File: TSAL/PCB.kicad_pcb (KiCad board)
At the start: 4 copper layers, 29.2 x 51.1 mm, 35 parts, among them J1 Conn_01x15, J2 USB_C_Receptacle_USB2.0, J3 Conn_01x15, J4 TC2030, J5 Conn_01x04, SW1 SW_Push, SW2 SW_Push, U1 SN65HVD230, U2 AMS1117-3.3, U3 STM32F103C8T6, Y1 8MHz

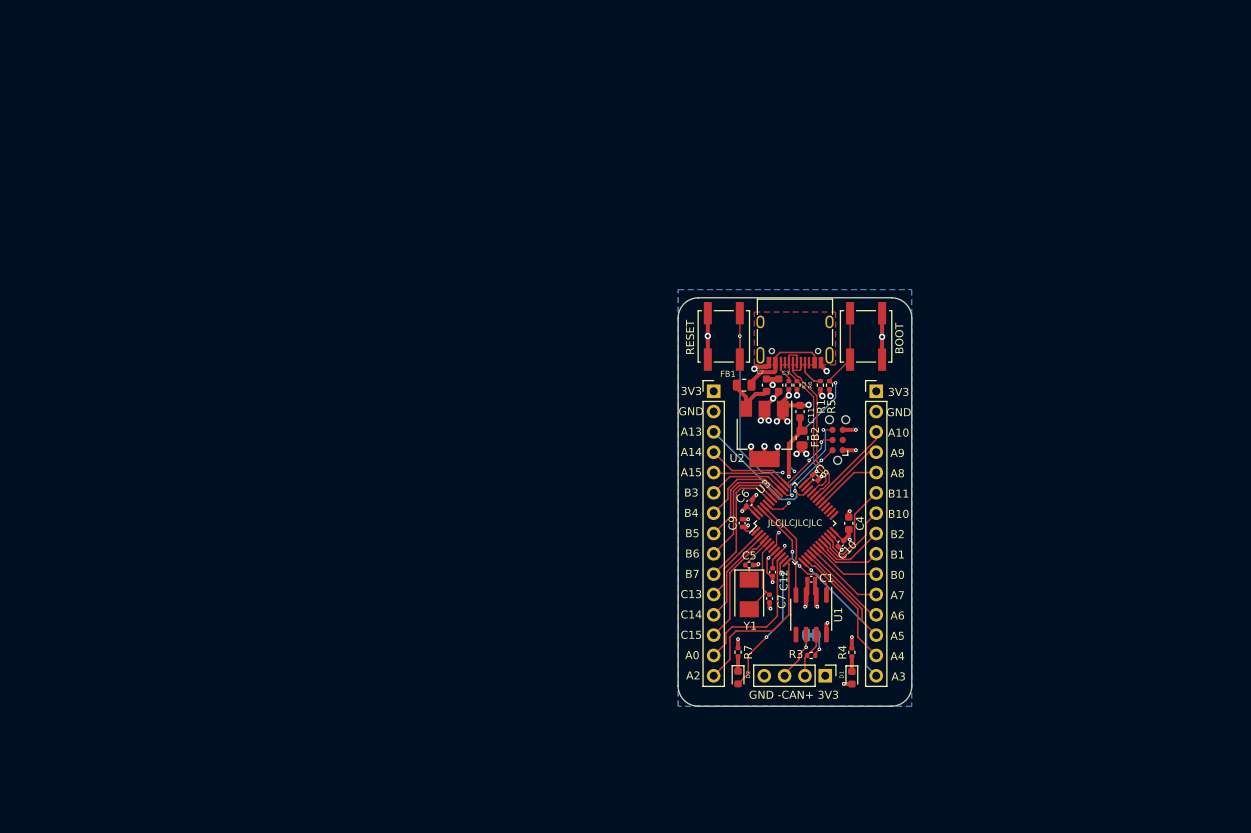
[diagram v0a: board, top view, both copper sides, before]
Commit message: Changed opto-isolator
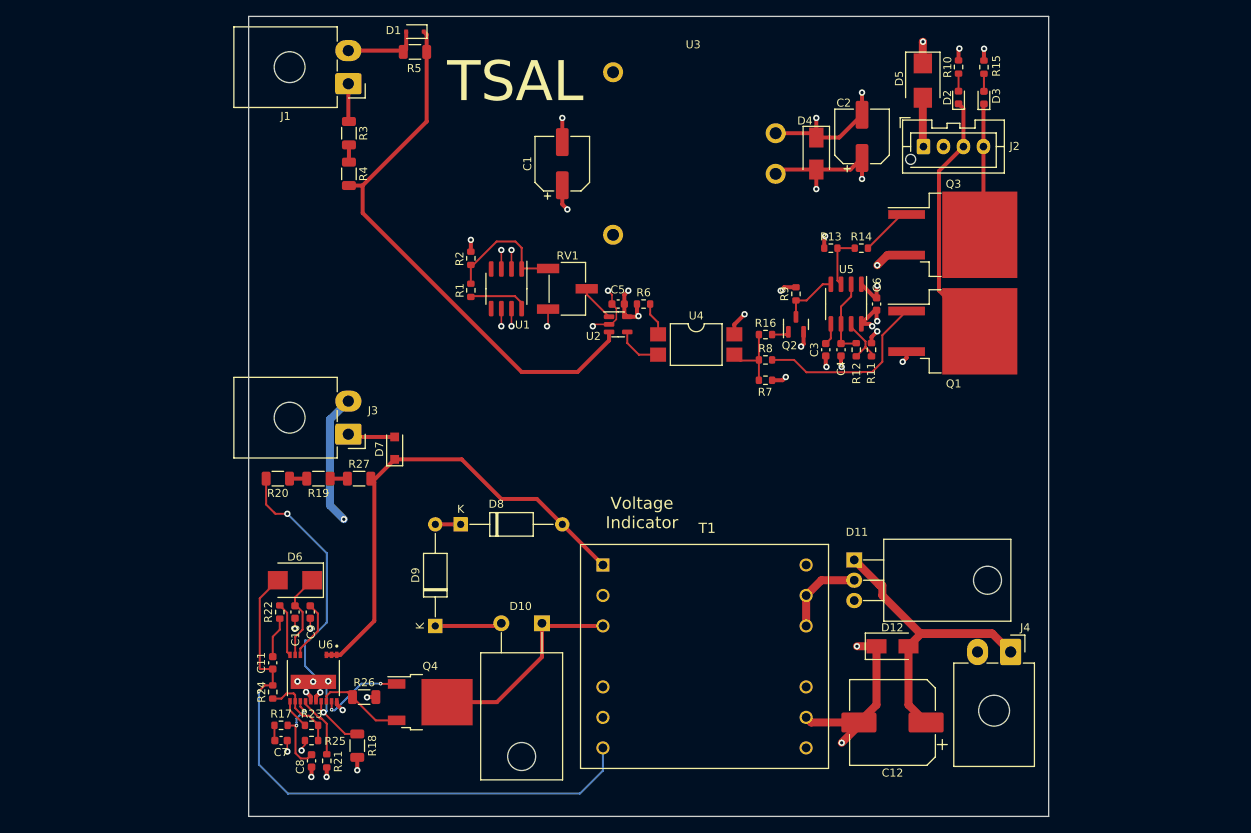
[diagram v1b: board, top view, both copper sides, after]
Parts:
- removed FB1, FB2: 100R@100MHz, Resistor_SMD:R_0805_2012Metric
- removed J5: Conn_01x04, Connector_PinHeader_2.54mm:PinHeader_1x04_P2.54mm_Vertical
- removed JP1: SolderJumper_Bridged, Jumper:SolderJumper-2_P1.3mm_Bridged_RoundedPad1.0x1.5mm
- removed SW1, SW2: SW_Push, Button_Switch_SMD:SW_Push_1P1T_NO_CK_KSC7xxJ
- removed Y1: 8MHz, Crystal:Crystal_SMD_5032-2Pin_5.0x3.2mm
- added D10: RFN5TF8S, Package_TO_SOT_THT:TO-220-2_Horizontal_TabDown, F.Cu at (115.7, 117.9)
- added D11: RB238T150, Package_TO_SOT_THT:TO-220-3_Horizontal_TabDown, F.Cu at (154.7, 110.0)
- added D12: SMAJ15CA, Diode_SMD:D_SMA, F.Cu at (159.5, 120.8)
- added D3: LED-Red, LED_SMD:LED_0603_1608Metric, F.Cu at (170.9, 52.2)
- added D4: SMAJ15CA, Diode_SMD:D_SMA, F.Cu at (150.0, 59.2)
- added D5: SSB43L, Diode_SMD:D_SMB, F.Cu at (163.3, 50.1)
- added D6: SK520B, Diode_SMD:D_SMB, F.Cu at (84.8, 112.5)
- added D7: 1N4007FL, Diode_SMD:D_SOD-123F, F.Cu at (97.3, 96.0)
- added D8: 1N5375B, Diode_THT:D_A-405_P12.70mm_Horizontal, F.Cu at (105.5, 105.5)
- added D9: 1N5375B, Diode_THT:D_A-405_P12.70mm_Horizontal, F.Cu at (102.4, 118.2)
- added Q1: IRLZ44N, Package_TO_SOT_SMD:TO-263-2, F.Cu at (167.0, 81.4)
- added Q2: MMBT3904, Package_TO_SOT_SMD:SOT-23, F.Cu at (147.4, 80.5)
- added Q3: IRLZ44N, Package_TO_SOT_SMD:TO-263-2, F.Cu at (167.0, 69.3)
- added Q4: STD7NK40Z, Package_TO_SOT_SMD:TO-252-2, F.Cu at (101.7, 127.8)
- added R10: 2.2k, Resistor_SMD:R_0603_1608Metric, F.Cu at (167.8, 48.4)
- added R11: 22k, Resistor_SMD:R_0603_1608Metric, F.Cu at (156.9, 83.7)
- added R12: 220k, Resistor_SMD:R_0603_1608Metric, F.Cu at (155.0, 83.7)
- added R13: 100k, Resistor_SMD:R_0603_1608Metric, F.Cu at (151.8, 71.0)
- added R14: 1k, Resistor_SMD:R_0603_1608Metric, F.Cu at (155.6, 71.0)
- added R15: 2.2k, Resistor_SMD:R_0603_1608Metric, F.Cu at (170.9, 48.4)
- added R16: 22k, Resistor_SMD:R_0603_1608Metric, F.Cu at (143.6, 81.8)
- added R17: 10k, Resistor_SMD:R_0603_1608Metric, F.Cu at (83.1, 130.7)
- added R18: 40k, Resistor_SMD:R_1206_3216Metric, F.Cu at (92.6, 133.2)
- added R19: 500k, Resistor_SMD:R_1206_3216Metric, F.Cu at (87.8, 99.8)
- added R20: 500k, Resistor_SMD:R_1206_3216Metric, F.Cu at (82.7, 99.8)
- added R21: 56.2k, Resistor_SMD:R_0603_1608Metric, F.Cu at (88.8, 135.1)
- added R22: 10k, Resistor_SMD:R_0603_1608Metric, F.Cu at (82.9, 116.5)
- added R23: 121k, Resistor_SMD:R_0603_1608Metric, F.Cu at (86.9, 130.7)
- added R24: 44.2k, Resistor_SMD:R_0603_1608Metric, F.Cu at (82.0, 126.5)
- added R25: 4.99k, Resistor_SMD:R_0603_1608Metric, F.Cu at (86.9, 132.6)
- added R26: 0.05, Resistor_SMD:R_1206_3216Metric, F.Cu at (93.5, 127.1)
- added R27: 500k, Resistor_SMD:R_1206_3216Metric, F.Cu at (92.8, 99.8)
- added R8: 1k, Resistor_SMD:R_0603_1608Metric, F.Cu at (143.6, 85.0)
- added R9: 22k, Resistor_SMD:R_0603_1608Metric, F.Cu at (147.4, 76.7)
- added RV1: 10k, Potentiometer_SMD:Potentiometer_Bourns_3269W_Vertical, F.Cu at (118.9, 76.1)
- added T1: 11328-T078, 11328-T078:11328T078, F.Cu at (123.3, 110.6)
- added U4: LTV-817S, Package_DIP:SMDIP-4_W9.53mm, F.Cu at (135.0, 83.1)
- added U5: LM555xN, Package_SO:SOIC-8_3.9x4.9mm_P1.27mm, F.Cu at (153.7, 78.0)
- added U6: LT8316IFE#PBF, kicad-libraries:IC_LT8316IFE#PBF, F.Cu at (87.1, 124.8)
- C1: value 100n -> 100u; footprint Capacitor_SMD:C_0402_1005Metric -> Capacitor_SMD:CP_Elec_6.3x7.7
- C10, C9: value 100n -> 4.7u; footprint Capacitor_SMD:C_0402_1005Metric -> Capacitor_SMD:C_0603_1608Metric
- C11: value 1u -> 47p
- C12: value 100n -> 470uF; footprint Capacitor_SMD:C_0402_1005Metric -> Capacitor_SMD:CP_Elec_10x10.5
- C2: value 1u -> 100u; footprint Capacitor_SMD:C_0603_1608Metric -> Capacitor_SMD:CP_Elec_6.3x7.7
- C3: value 1u -> 100nF
- C4: value 4u7 -> 1microF
- C5: value 30p -> 100nF; footprint Capacitor_SMD:C_0402_1005Metric -> Capacitor_SMD:C_0603_1608Metric
- C6: value 100n -> 100nF; footprint Capacitor_SMD:C_0402_1005Metric -> Capacitor_SMD:C_0603_1608Metric
- C7: value 30p -> 0.1u; footprint Capacitor_SMD:C_0402_1005Metric -> Capacitor_SMD:C_0603_1608Metric
- C8: value 100n -> 47p; footprint Capacitor_SMD:C_0402_1005Metric -> Capacitor_SMD:C_0603_1608Metric
- D1: value YELLOW -> BZT52C5V1SQ-7-F; footprint LED_SMD:LED_0603_1608Metric -> Diode_SMD:D_SOD-323F
- D2: value BLUE -> LED-Green
- J1, J3: value Conn_01x15 -> TE 770966-2; footprint Connector_PinHeader_2.54mm:PinHeader_1x15_P2.54mm_Vertical -> Connector_TE-Connectivity:TE_MATE-N-LOK_1-770966-x_1x02_P4.14mm_Horizontal
- J2: value USB_C_Receptacle_USB2.0 -> JST B04B-XASK; footprint Connector_USB:USB_C_Receptacle_HRO_TYPE-C-31-M-12 -> Connector_JST:JST_XA_B04B-XASK-1-A_1x04_P2.50mm_Vertical
- J4: value TC2030 -> TE 770966-2; footprint Connector:Tag-Connect_TC2030-IDC-NL_2x03_P1.27mm_Vertical -> Connector_TE-Connectivity:TE_MATE-N-LOK_1-770966-x_1x02_P4.14mm_Horizontal
- R1, R2: value 5k1 -> 2.2k; footprint Resistor_SMD:R_0402_1005Metric -> Resistor_SMD:R_0603_1608Metric
- R3: value 120R -> 1M; footprint Resistor_SMD:R_0402_1005Metric -> Resistor_SMD:R_1206_3216Metric
- R4: value 1k5 -> 1M; footprint Resistor_SMD:R_0402_1005Metric -> Resistor_SMD:R_1206_3216Metric
- R5: value 5k1 -> 20K; footprint Resistor_SMD:R_0402_1005Metric -> Resistor_SMD:R_1206_3216Metric
- R6: value 1k5 -> 2.2k; footprint Resistor_SMD:R_0402_1005Metric -> Resistor_SMD:R_0603_1608Metric
- R7: value 1k5 -> 100k; footprint Resistor_SMD:R_0402_1005Metric -> Resistor_SMD:R_0603_1608Metric
- U1: value SN65HVD230 -> TL431D
- U2: value AMS1117-3.3 -> LMV331; footprint Package_TO_SOT_SMD:SOT-223-3_TabPin2 -> Package_TO_SOT_SMD:SOT-23-5
- U3: value STM32F103C8T6 -> VRB1205YMD-6WR3; footprint Package_QFP:LQFP-48_7x7mm_P0.5mm -> VRB1205YMD-6WR3:VRB1205YMD-6WR3
- moved D1 97.5 mm to (99.8, 43.9), turned to 180 degrees
- moved R3 87.2 mm to (91.6, 56.6), turned to -90 degrees
- moved R4 86.8 mm to (91.6, 61.7), turned to -90 degrees
- moved D2 77.6 mm to (167.8, 52.2), turned to 90 degrees
- moved C11 73.0 mm to (82.0, 122.8)
- moved C8 72.2 mm to (86.9, 135.1), turned to -90 degrees
- moved C10 68.7 mm to (84.8, 116.5), turned to 90 degrees
- moved R5 66.5 mm to (99.8, 46.5), turned to 180 degrees
- moved J3 66.2 mm to (91.5, 94.3), turned to 180 degrees
- moved C7 63.6 mm to (83.1, 132.6), turned to 0 degrees
- moved C1 60.5 mm to (118.2, 60.5), turned to 90 degrees
- moved J1 59.7 mm to (91.5, 50.5), turned to 180 degrees
- moved U1 55.8 mm to (111.3, 76.1)
- moved C9 55.1 mm to (86.7, 116.5)
- moved U3 47.9 mm to (134.7, 59.2), turned to 180 degrees
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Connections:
- C1 pad 1: +3V3 -> +5V
- C1 pad 2: GND -> TS-
- C10 pad 1: +3V3 -> VI-
- C10 pad 2: GND -> Net-(C10-Pad2)
- C11 pad 1: +3.3VA -> Net-(C11-Pad1)
- C11 pad 2: GND -> Net-(C11-Pad2)
- C12 pad 1: +3.3VA -> Net-(C12-Pad1)
- C2 pad 1: VCC -> +12V
- C3 pad 1: +3V3 -> GND
- C3 pad 2: GND -> Net-(C3-Pad2)
- C4 pad 1: +3V3 -> Net-(C4-Pad1)
- C5 pad 1: /HSE_OUT -> +5V
- C5 pad 2: GND -> TS-
- C6 pad 1: +3V3 -> +12V
- C7 pad 1: /HSE_IN -> Net-(C7-Pad1)
- C7 pad 2: GND -> VI-
- C8 pad 1: +3V3 -> Net-(C8-Pad1)
- C8 pad 2: GND -> VI-
- C9 pad 1: +3V3 -> VI-
- C9 pad 2: GND -> Net-(C9-Pad2)
- D1 pad 2: +3V3 -> TS-
- D2 pad 1: Net-(D2-Pad1) -> /Ext-LED-Green
- D2 pad 2: /LED_STAT -> Net-(D2-Pad2)
- J1 pad 1: +3V3 -> TS+
- J1 pad 2: GND -> TS-
- J3 pad 1: +3V3 -> Net-(D7-Pad2)
- J3 pad 2: GND -> VI-
- J4 pad 1: +3V3 -> Net-(C12-Pad1)
- J4 pad 2: SWDIO -> GND
- R1 pad 1: Net-(J2-PadA5) -> Net-(R1-Pad1)
- R1 pad 2: GND -> Net-(R1-Pad2)
- R2 pad 1: GND -> +5V
- R2 pad 2: Net-(J2-PadB5) -> Net-(R1-Pad1)
- R3 pad 1: /CAN+ -> TS+
- R3 pad 2: Net-(JP1-Pad2) -> Net-(R3-Pad2)
- R4 pad 1: Net-(D1-Pad1) -> Net-(R3-Pad2)
- R4 pad 2: GND -> Net-(D1-Pad1)
- R5 pad 1: /BOOT0 -> Net-(D1-Pad1)
- R5 pad 2: GND -> TS-
- R6 pad 1: +3V3 -> +5V
- R6 pad 2: USB_D+ -> Net-(R6-Pad2)
- R7 pad 1: Net-(D2-Pad1) -> Net-(R16-Pad1)
- U1 pad 1: CANTX -> Net-(R1-Pad1)
- U1 pad 2: GND -> TS-
- U1 pad 3: +3V3 -> TS-
- U1 pad 4: CANRX -> (no net)
- U1 pad 5: unconnected-(U1-Pad5) -> (no net)
- U1 pad 6: /CAN- -> TS-
- U1 pad 7: /CAN+ -> TS-
- U1 pad 8: GND -> Net-(R1-Pad2)
- U2 pad 1: GND -> Net-(RV1-Pad2)
- U2 pad 2: +3V3 -> TS-
- U2 pad 3: VCC -> Net-(D1-Pad1)
- U3 pad 1: +3V3 -> GND
- U3 pad 2: PC13 -> +12V
- U3 pad 3: PC14 -> +5V
- U3 pad 5: /HSE_OUT -> TS-
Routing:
- net Net-(C11-Pad1): track 0.00 -> 75.4 mm, vias 0 -> 1
- net Net-(D1-Pad1): track 1.88 -> 69.6 mm
- net VI+: track 0.00 -> 61.2 mm
- net Net-(C12-Pad1): track 0.00 -> 46.6 mm
- net +3V3: track 44.0 -> 0.00 mm, vias 18 -> 0
- net Net-(R18-Pad2): track 0.00 -> 42.9 mm, vias 0 -> 2
- net /NRST: track 35.9 -> 0.00 mm, vias 3 -> 0
- net +12V: track 0.00 -> 34.8 mm, vias 0 -> 10
- net /Ext-LED-Green: track 0.00 -> 32.1 mm
- net /BOOT0: track 31.5 -> 0.00 mm, vias 3 -> 0
- net TS-: track 0.00 -> 31.3 mm, vias 0 -> 8
- net VI-: track 0.00 -> 31.2 mm, vias 0 -> 15
- net Net-(D10-Pad1): track 0.00 -> 26.2 mm
- net SWDIO: track 24.1 -> 0.00 mm, vias 2 -> 0
- net SWO: track 22.9 -> 0.00 mm, vias 2 -> 0
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- added copper zone on In2.Cu, net +12V
- added copper zone on In2.Cu, net +5V
- added copper zone on In1.Cu, net TS-
- added copper zone on In1.Cu, net VI-
- removed copper zone on In2.Cu, net +3V3
- removed copper zone on B.Cu, net GND
- removed copper zone on F.Cu, net unconnected-(J2-PadS1)
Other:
- board size 29.2 x 51.1 mm -> 100 x 100 mm
- board text added: "TSAL"
- board text added: "Voltage Indicator"
- board text removed: "3V3"
- board text removed: "3V3 +CAN- GND"
- board text removed: "A0"
- board text removed: "A10"
- board text removed: "A13"
- board text removed: "A14"
- board text removed: "A15"
- board text removed: "A2"
- board text removed: "A3"
- board text removed: "A4"
- board text removed: "A5"
- board text removed: "A6"
- board text removed: "A7"
- board text removed: "A8"
- board text removed: "A9"
- board text removed: "B0"
- board text removed: "B1"
- board text removed: "B10"
- board text removed: "B11"
- board text removed: "B2"
- board text removed: "B3"
- board text removed: "B4"
- board text removed: "B5"
- board text removed: "B6"
- board text removed: "B7"
- board text removed: "BOOT"
- board text removed: "C13"
- board text removed: "C14"
- board text removed: "C15"
- board text removed: "CAN TERM"
- board text removed: "GND"
- board text removed: "GND -CAN+ 3V3"
- board text removed: "JLCJLCJLCJLC"
- board text removed: "RESET"
- board text removed: "Rev 1"
- board text removed: "STM32F103 CAN/USB-C Jack LeFevre July 2022"
- board text removed: "SWCLK"
- board text removed: "SWDIO"
- board text removed: "SWO"

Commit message: TSAL - meme
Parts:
- added REF**: MountingHole_3.2mm_M3_ISO14580, MountingHole:MountingHole_3.2mm_M3_ISO14580, F.Cu at (156.0, 139.0)
- added REF**: MountingHole_3.2mm_M3_ISO14580, MountingHole:MountingHole_3.2mm_M3_ISO14580, F.Cu at (170.0, 98.0)
- added REF**: MountingHole_3.2mm_M3_ISO14580, MountingHole:MountingHole_3.2mm_M3_ISO14580, F.Cu at (86.0, 75.0)
- added REF**: MountingHole_3.2mm_M3_ISO14580, MountingHole:MountingHole_3.2mm_M3_ISO14580, F.Cu at (154.0, 47.0)
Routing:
- net Net-(R18-Pad2): track 42.9 -> 40.9 mm
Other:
- board text added: "12V GND GRN RED"
- board text added: "Bronco Racing TSAL + Voltage Indicator Rev 1"
- board text added: "GND"
- board text added: "Grounded Low Voltage"
- board text added: "High Voltage"
- board text added: "Josh Iwick Feb 2023"
- board text added: "TS+"
- board text added: "TS-"
- board text added: "TSAL HV In"
- board text added: "VI 12V"
- board text added: "Voltage Indicator In"

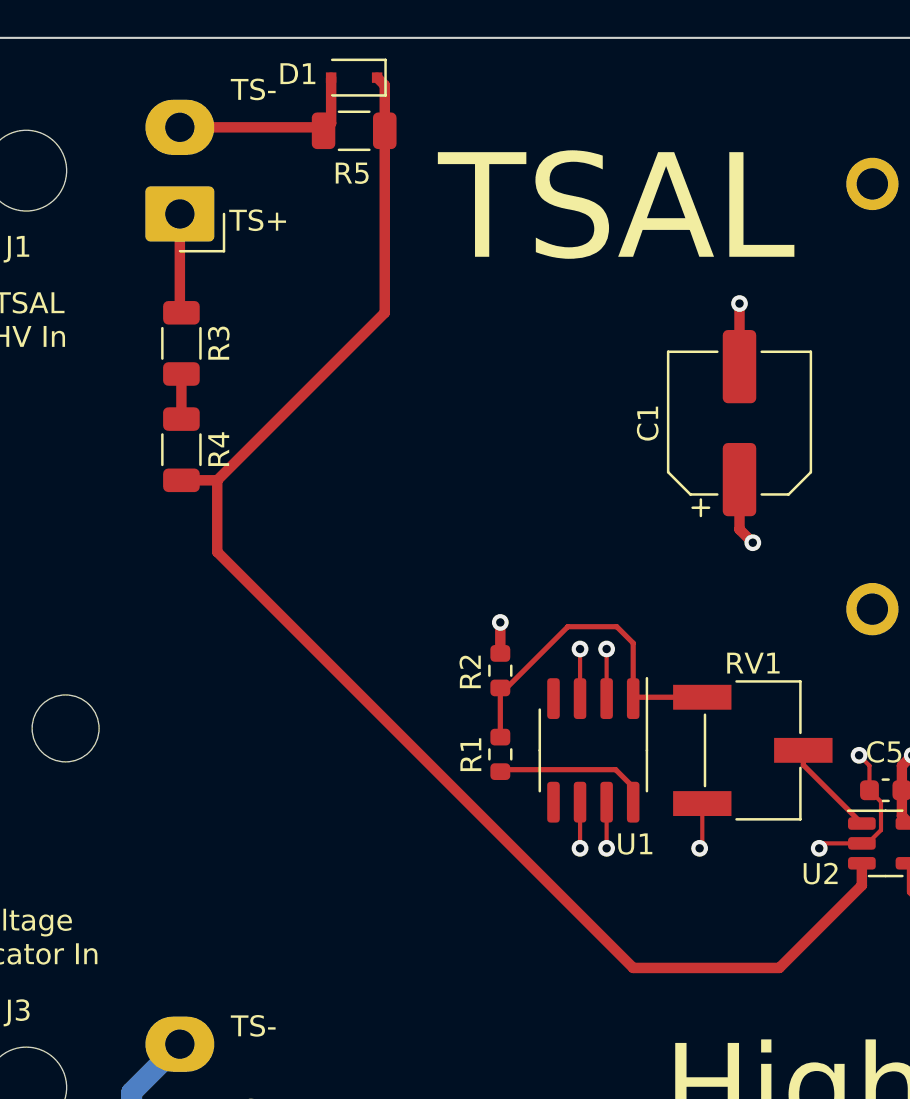
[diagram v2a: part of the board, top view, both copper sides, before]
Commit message: resisitor change
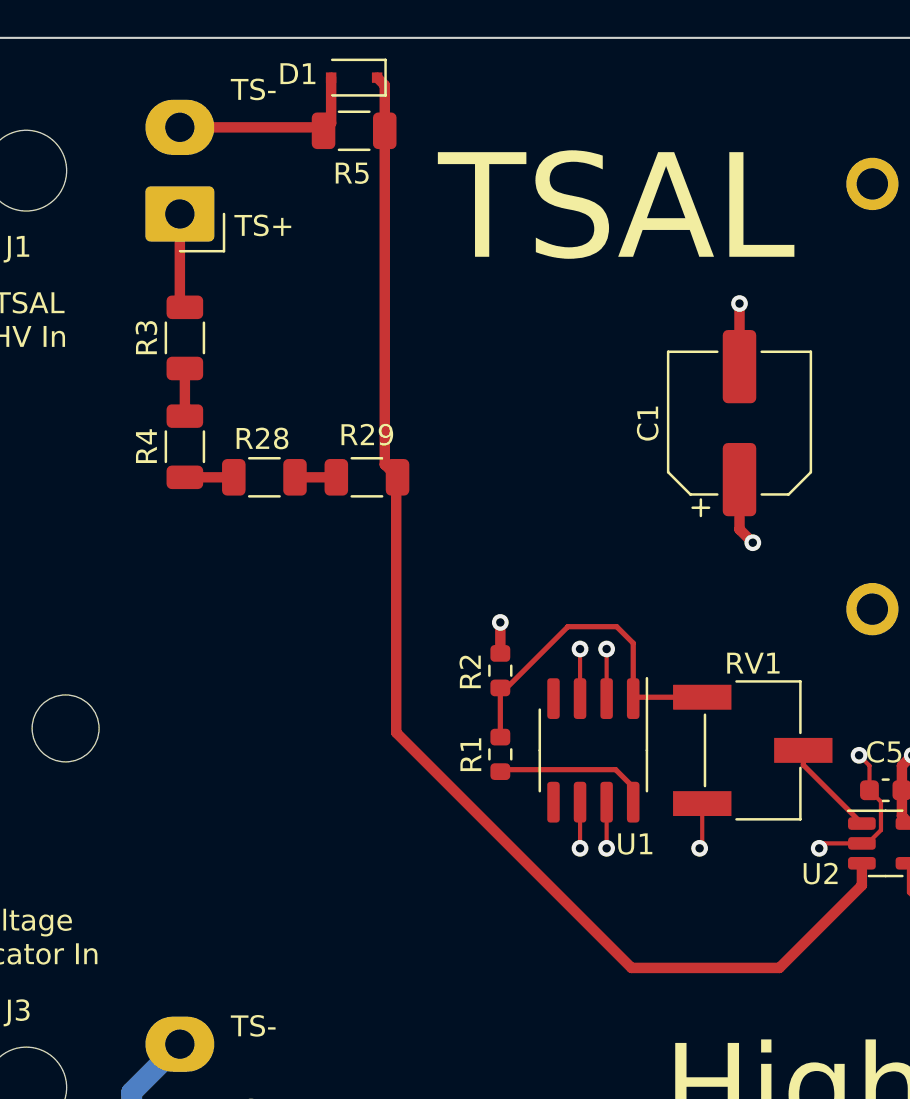
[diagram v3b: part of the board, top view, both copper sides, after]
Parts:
- added R28: 500k, Resistor_SMD:R_1206_3216Metric, F.Cu at (95.5, 63.0)
- added R29: 500k, Resistor_SMD:R_1206_3216Metric, F.Cu at (100.4, 63.0)
- C4: value 1microF -> 1u
- C7: value 0.1u -> 100nF
- R3, R4: value 1M -> 500k
- moved R3 0.31 mm to (91.7, 56.4)
- moved R4 0.22 mm to (91.7, 61.6)
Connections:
- R4 pad 2: Net-(D1-Pad1) -> Net-(R28-Pad1)
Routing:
- net Net-(D1-Pad1): track 69.6 -> 61.3 mm
- net Net-(R28-Pad1): track 0.00 -> 2.34 mm
- net Net-(R28-Pad2): track 0.00 -> 1.97 mm

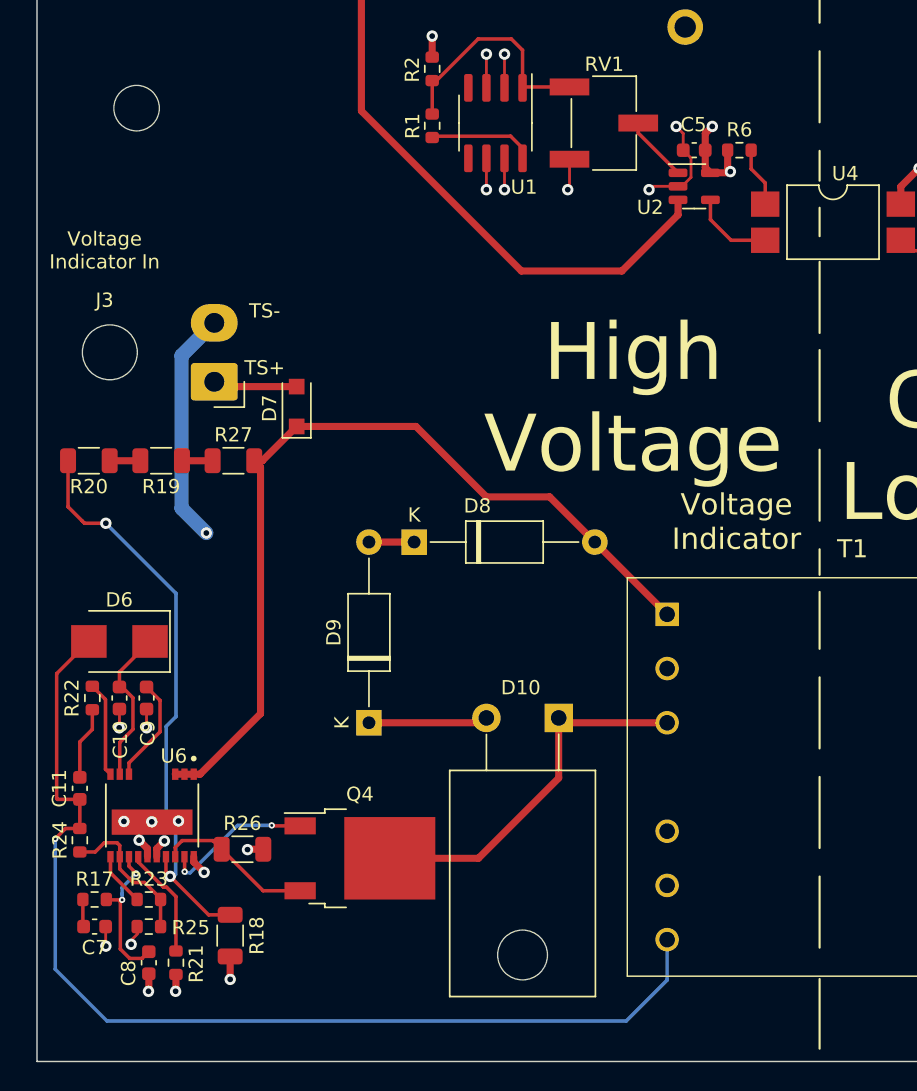
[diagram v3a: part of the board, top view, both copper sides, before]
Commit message: Fixed drc violations
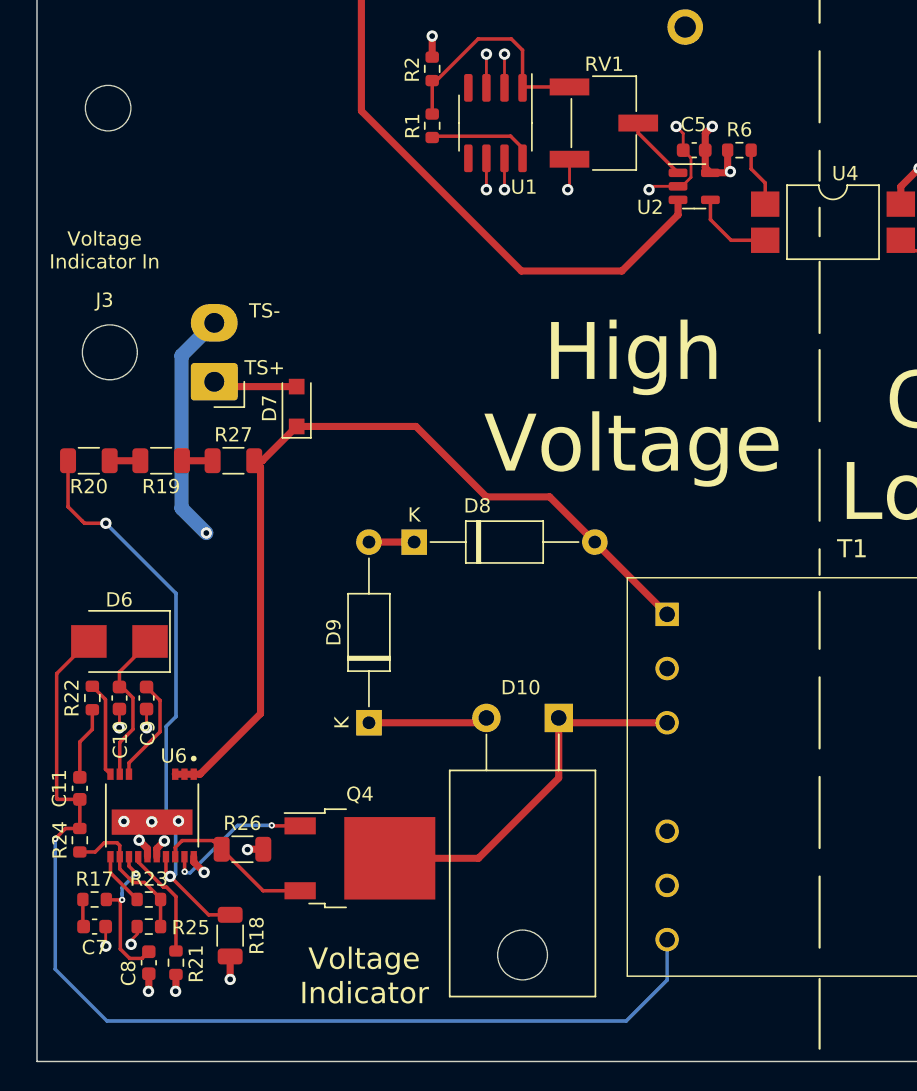
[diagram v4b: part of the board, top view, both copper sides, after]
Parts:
- moved H1 2.00 mm to (84.0, 75.0)
- renumbered REF** to H1, REF** to H2, REF** to H3, REF** to H4
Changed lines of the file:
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@@
     (tags "mounting hole 3.2mm no annular m3 iso14580")
     (attr exclude_from_pos_files exclude_from_bom)
-    (fp_text reference "REF**" (at 0 -3.75) (layer "F.SilkS") hide
+    (fp_text reference "H4" (at 0 -3.75) (layer "F.SilkS") hide
       (effects (font (size 1 1) (thickness 0.15)))
     )
@@
     (tags "mounting hole 3.2mm no annular m3 iso14580")
     (attr exclude_from_pos_files exclude_from_bom)
-    (fp_text reference "REF**" (at 0 -3.75) (layer "F.SilkS") hide
+    (fp_text reference "H3" (at 0 -3.75) (layer "F.SilkS") hide
       (effects (font (size 1 1) (thickness 0.15)))
     )
@@
   )
   (footprint "MountingHole:MountingHole_3.2mm_M3_ISO14580" (layer "F.Cu")
-    (at 86.032 75.042)
+    (at 84.032 75.042)
     (descr "Mounting Hole 3.2mm, no annular, M3, ISO14580")
     (tags "mounting hole 3.2mm no annular m3 iso14580")
     (attr exclude_from_pos_files exclude_from_bom)
-    (fp_text reference "REF**" (at 0 -3.75) (layer "F.SilkS") hide
+    (fp_text reference "H1" (at 0 -3.75) (layer "F.SilkS") hide
       (effects (font (size 1 1) (thickness 0.15)))
     )
@@
     (tags "mounting hole 3.2mm no annular m3 iso14580")
     (attr exclude_from_pos_files exclude_from_bom)
-    (fp_text reference "REF**" (at 0 -3.75) (layer "F.SilkS") hide
+    (fp_text reference "H2" (at 0 -3.75) (layer "F.SilkS") hide
       (effects (font (size 1 1) (thickness 0.15)))
     )
@@
     (effects (font (size 1 1) (thickness 0.25)))
   )
-  (gr_text "Voltage \nIndicator" (at 128.1938 104.1146) (layer "F.SilkS")
+  (gr_text "Voltage \nIndicator" (at 102.032 136.042) (layer "F.SilkS")
     (effects (font (size 1.5 1.5)))
   )
@@
     (connect_pads (clearance 0))
     (min_thickness 0.254)
-    (keepout (tracks not_allowed) (vias not_allowed) (pads not_allowed) (copperpour not_allowed) (footprints allowed))
+    (keepout (tracks not_allowed) (vias not_allowed) (pads allowed) (copperpour not_allowed) (footprints allowed))
     (fill (thermal_gap 0.508) (thermal_bridge_width 0.508))
     (polygon

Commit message: TSAL W/ updated DC-DC + Meme
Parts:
- added G***: LOGO, TSAL:pika, B.Cu at (107.9, 59.7)
- U3: value VRB1205YMD-6WR3 -> VRB1205YMD-15WR3; footprint VRB1205YMD-6WR3:VRB1205YMD-6WR3 -> VRB1205YMD-6WR3:VRB1205YMD-15WR3
- moved U3 0.06 mm to (134.7, 59.2)
- turned C2 to -90 degrees
- turned D4 to 90 degrees
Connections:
- U3 pad 1: GND -> +12V
- U3 pad 2: +12V -> GND
- U3 pad 3: +5V -> +12V
- U3 pad 5: TS- -> unconnected-(U3-Pad5)
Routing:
- net +5V: track 11.4 -> 32.2 mm
- net GND: track 58.6 -> 57.9 mm
- net +12V: track 34.8 -> 35.5 mm
